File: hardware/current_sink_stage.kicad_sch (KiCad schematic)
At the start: 18 parts, among them Q1 NMOS, U1 AD8602, U2 ADTL084

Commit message: Updates to structure of the schematic. Minor funcitonality adjustments.
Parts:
- removed Q1: NMOS, symbol Simulation_SPICE:NMOS
- added C1: 1u, Capacitor_SMD:C_0805_2012Metric_Pad1.18x1.45mm_HandSolder, symbol Device:C_Small
- added C1: ?, Capacitor_SMD:C_0805_2012Metric_Pad1.18x1.45mm_HandSolder, symbol Device:C_Small
- added Q1, Q3: TK7S10N1Z, Package_TO_SOT_SMD:TO-252-2, symbol User_MOSFET:TK7S10N1Z
- added R1 (x4): 0, Resistor_SMD:R_0805_2012Metric_Pad1.20x1.40mm_HandSolder, symbol Device:R_Small
- added R1, R5 (x5): 100, Resistor_SMD:R_0805_2012Metric_Pad1.20x1.40mm_HandSolder, symbol Device:R_Small
- added R10, R11, R7, R8, R9: 10k, Resistor_SMD:R_0805_2012Metric_Pad1.20x1.40mm_HandSolder, symbol Device:R_Small
- added R2, R6: 1k, Resistor_SMD:R_0805_2012Metric_Pad1.20x1.40mm_HandSolder, symbol Device:R_Small
- added R3: 100m, Resistor_SMD:R_1206_3216Metric_Pad1.30x1.75mm_HandSolder, symbol Device:R_Small
- added R4: 1.9k, Resistor_SMD:R_0805_2012Metric_Pad1.20x1.40mm_HandSolder, symbol Device:R_Small
- added RV1: PT10LV05, Potentiometer_THT:Potentiometer_Piher_PT-10-V05_Vertical, symbol Device:R_Potentiometer_Small
- added U1: AD8602, Package_SO:MSOP-8_3x3mm_P0.65mm, symbol User_Opamp:AD8602
- added U2 (x2): ADTL084, Package_SO:SOIC-14_3.9x8.7mm_P1.27mm, symbol User_Opamp:ADTL084
- C1: footprint (none) -> Capacitor_SMD:C_0805_2012Metric_Pad1.18x1.45mm_HandSolder
- R1, R10, R11, R2, R4, R5, R6, R7, R8, R9: footprint (none) -> Resistor_SMD:R_0805_2012Metric_Pad1.20x1.40mm_HandSolder
- R3: value 100 -> 100m; footprint (none) -> Resistor_SMD:R_1206_3216Metric_Pad1.30x1.75mm_HandSolder
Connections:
- net GND: now also R2.1, R3.1, R5.1, R5.1, R5.1, U2.10 (+), U2.5 (+)
- net at R1.2, R2.2: now also Q1.1 (G)
- net at R4.2, R7.2, U1.7: now also R5.2
- net at R11.2, U2.8: now also R1.1; no longer R1.1
- net current_feedback: now reaches R3.2, U1.5 (+)
- net current_feedback: now also Q1.3 (S), Q3.3 (S), R3.2, U1.5 (+)
- net supply_neg renamed -5V0_SUPPLY_G
- net -5V0_SUPPLY_G: now also C1.1, RV1.1
- net supply_pos renamed 5V0_SUPPLY_G
- net 5V0_SUPPLY_G: now also C1.2, RV1.3
- net voltage_set_ss renamed opStage1A_ang_g
- net opStage1A_ang_g: now also R1.1
- new net: C1.1, R9.1, U2.6 (-)
- new net: C1.2, R10.2, U2.7
- new net: R4.1, R5.2, R6.2, U1.6 (-)
- new net: R1.1, R11.2, U2.8
- new net: R10.1, R11.1, U2.9 (-)
- new net: R1.1, R1.2, R1.2 (x2)
- new net: R8.1, R9.2, U2.1
- new net: R7.1, R8.2, U2.2 (-)
- new net: R4.2, R5.2, R7.2, U1.7
- new net: Q3.1 (G), R1.2, R2.2
- new net: R6.1, RV1.2
- new net VOLTAGE_SINK_G: Q1.2 (D), Q3.2 (D)
- new net opStage1B_ang_g: R1.1, U2.3 (+)
- new net opStage2A_ang_g: R5.1, R5.2
- new net opStage2B_ang_g: R5.1, R5.2
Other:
- moved on the sheet: C1, R1, R10, R11, R2, R3, R4, R5, R6, R7, R8, R9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

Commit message: Began initial routing. Schematic still not fully complete.
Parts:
- renumbered Q1 to Q200, Q3 to Q201
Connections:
- net -5V0_SUPPLY_G: no longer U2.17 (V-)
- net current_feedback renamed current_feedback_A
- net current_feedback_A: no longer Q201.3 (S), R3.2, U1.5 (+)
- new net current_feedback_B: Q201.3 (S), R3.2, U1.5 (+)

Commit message: Routing close to completion. Pending review.
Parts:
- removed R6 (x2): 1k, Resistor_SMD:R_0805_2012Metric_Pad1.20x1.40mm_HandSolder, symbol Device:R_Small
- removed RV1 (x2): PT10LV05, Potentiometer_THT:Potentiometer_Piher_PT-10-V05_Vertical, symbol Device:R_Potentiometer_Small
- added TP500 (x4): ~, TestPoint:TestPoint_Pad_D1.0mm, symbol Connector:TestPoint
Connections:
- net opStage2A_ang_g: now also TP500.1
- net opStage2B_ang_g: now also TP500.1
- net at R1.1, R11.2, U2.8: now also TP500.1 (x2)

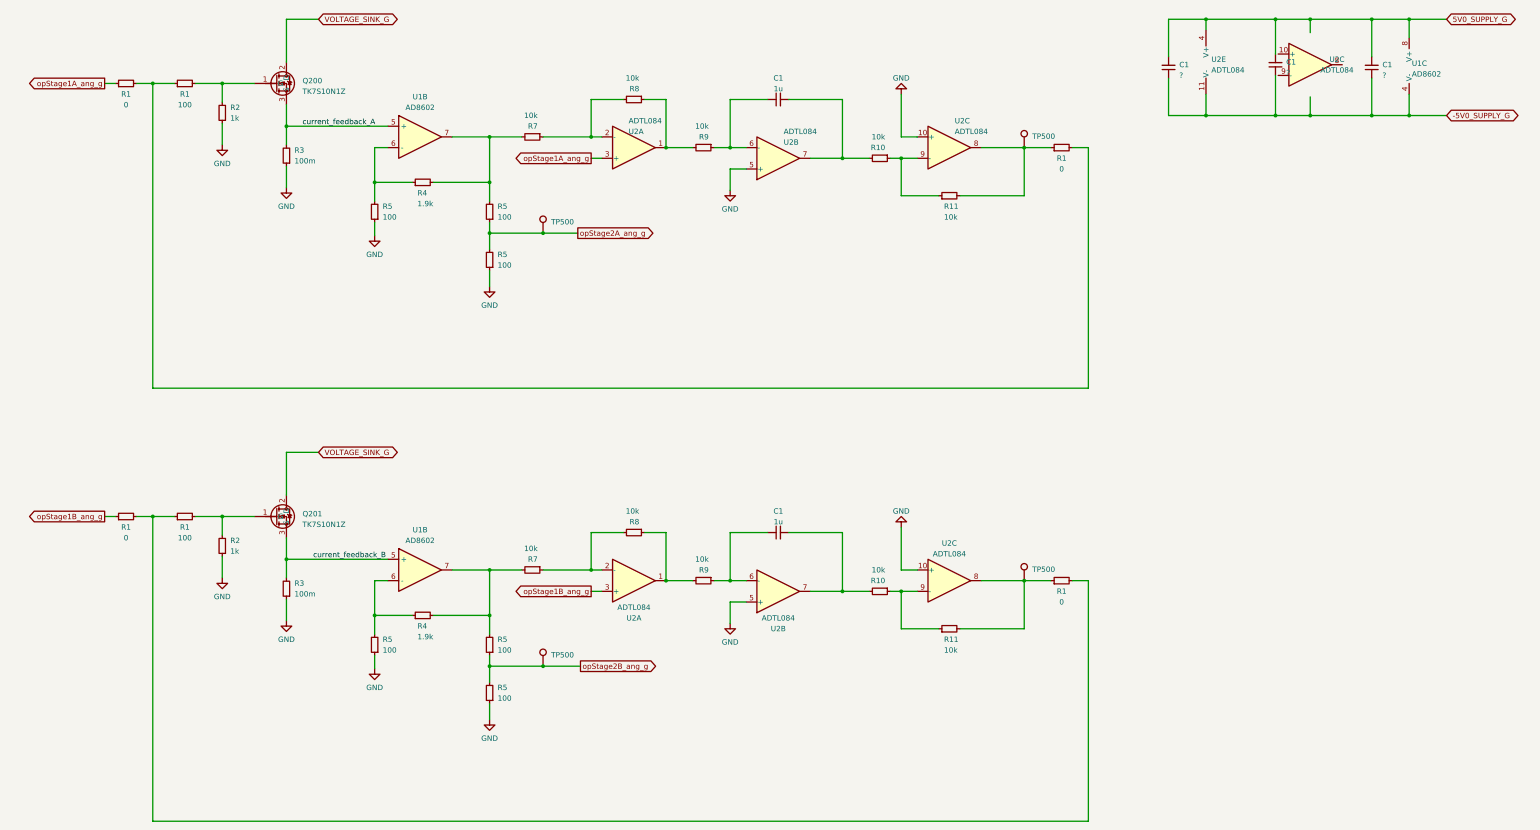
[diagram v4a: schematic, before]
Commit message: Added some doucmentation to MCP driver
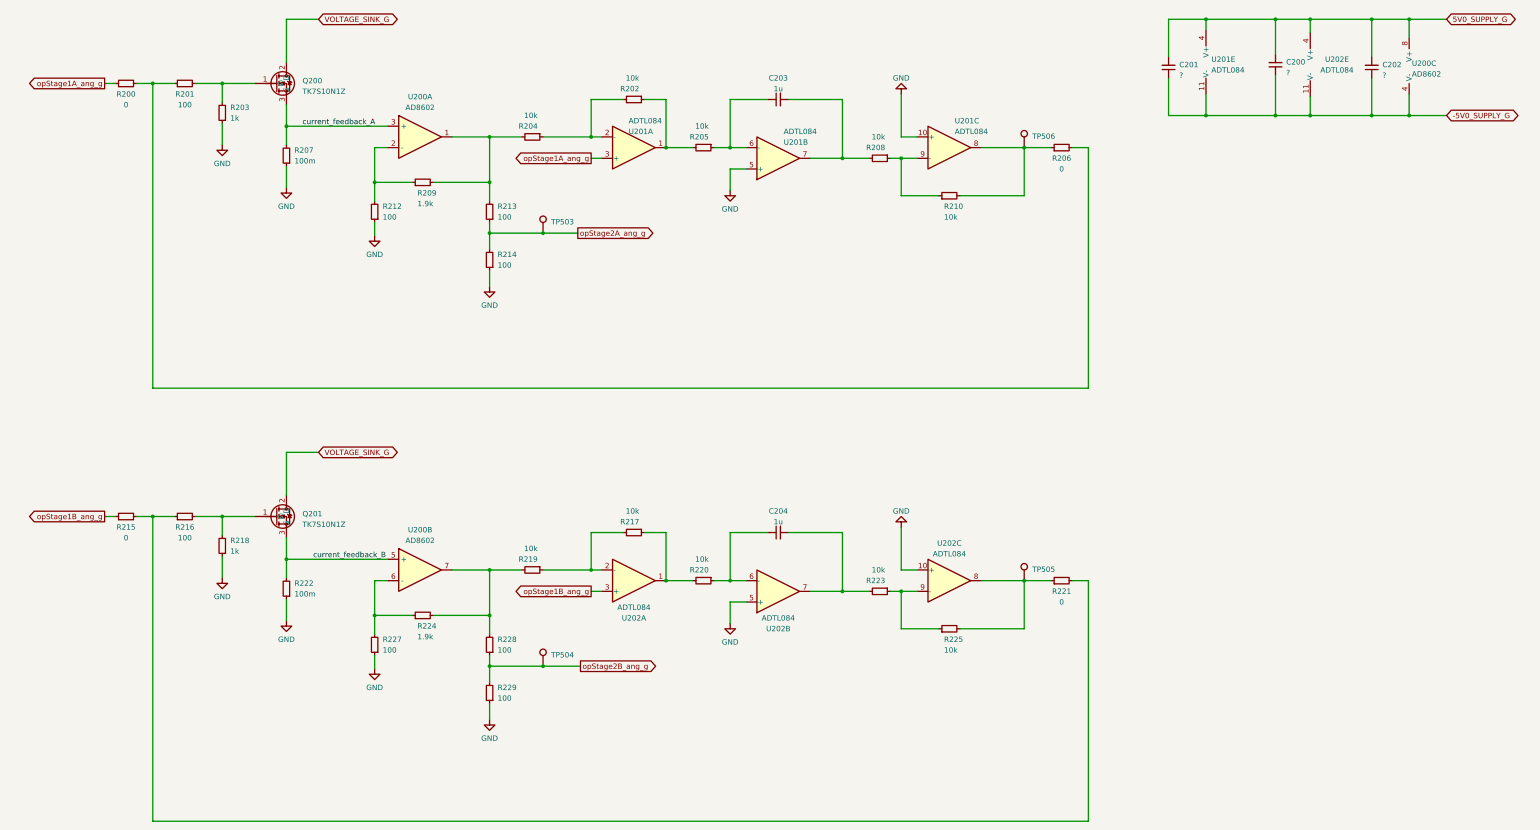
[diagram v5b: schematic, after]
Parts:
- renumbered C1 to C200, C1 to C201, C1 to C202, C1 to C203, C1 to C204, R1 to R200, R1 to R201, R8 to R202, R2 to R203, R7 to R204, R9 to R205, R1 to R206, R3 to R207, R10 to R208, R4 to R209, R11 to R210, R5 to R212, R5 to R213, R5 to R214, R1 to R215, R1 to R216, R8 to R217, R2 to R218, R7 to R219, R9 to R220, R1 to R221, R3 to R222, R10 to R223, R4 to R224, R11 to R225, R5 to R227, R5 to R228, R5 to R229, TP500 to TP503, TP500 to TP504, TP500 to TP505, TP500 to TP506, U1 to U200, U2 to U201, U2 to U202
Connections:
- net -5V0_SUPPLY_G: now also U202.11 (V-)
- net 5V0_SUPPLY_G: now also U202.4 (V+)
- net current_feedback_A: now also U200.3 (+); no longer U200.5 (+)
- net at R209.1, R212.2: now also U200.2 (-); no longer U200.6 (-)
- net at R204.2, R209.2, R213.2: now also U200.1; no longer U200.7
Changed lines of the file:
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@@
-(kicad_sch (version 20230121) (generator eeschema)
-  (paper "A3")
+(kicad_sch
+	(version 20231120)
+	(generator "eeschema")
+	(generator_version "8.0")
+	(paper "A3")
